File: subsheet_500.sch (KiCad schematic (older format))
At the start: 48 parts, among them J500 DM-15S — JOY0, J501 DM-15S — JOY1, U513 LM556_DUAL_TIMER_PHY, U514 LM556_DUAL_TIMER_PHY

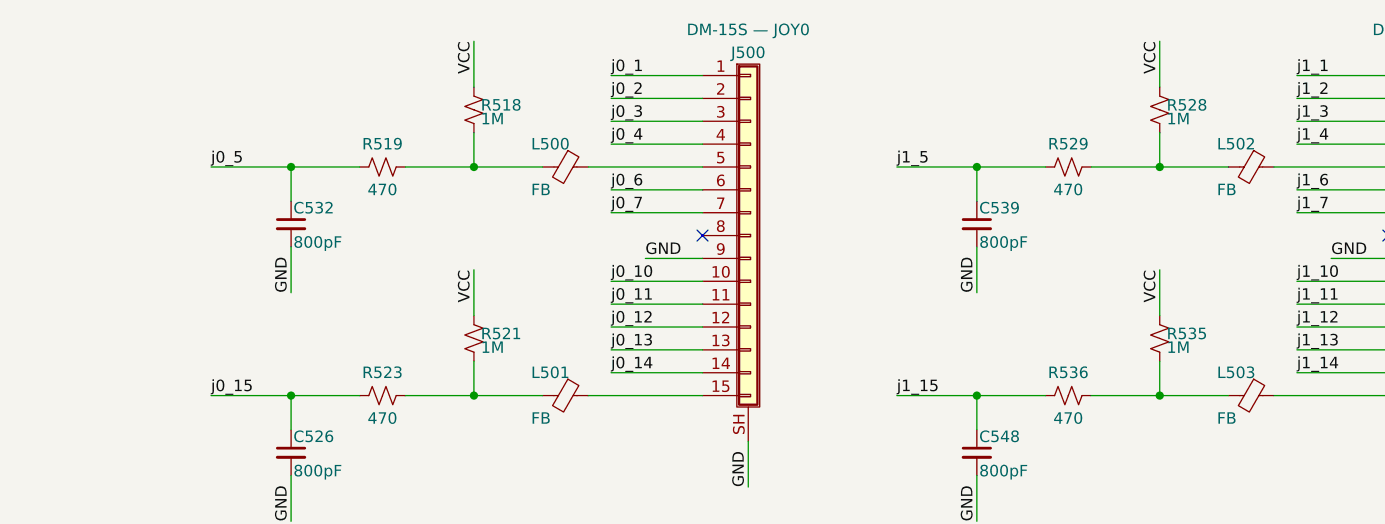
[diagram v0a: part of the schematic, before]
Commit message: [Schematics] added comment about the swap of the resistors between R518 and R521, and between R519 and R523
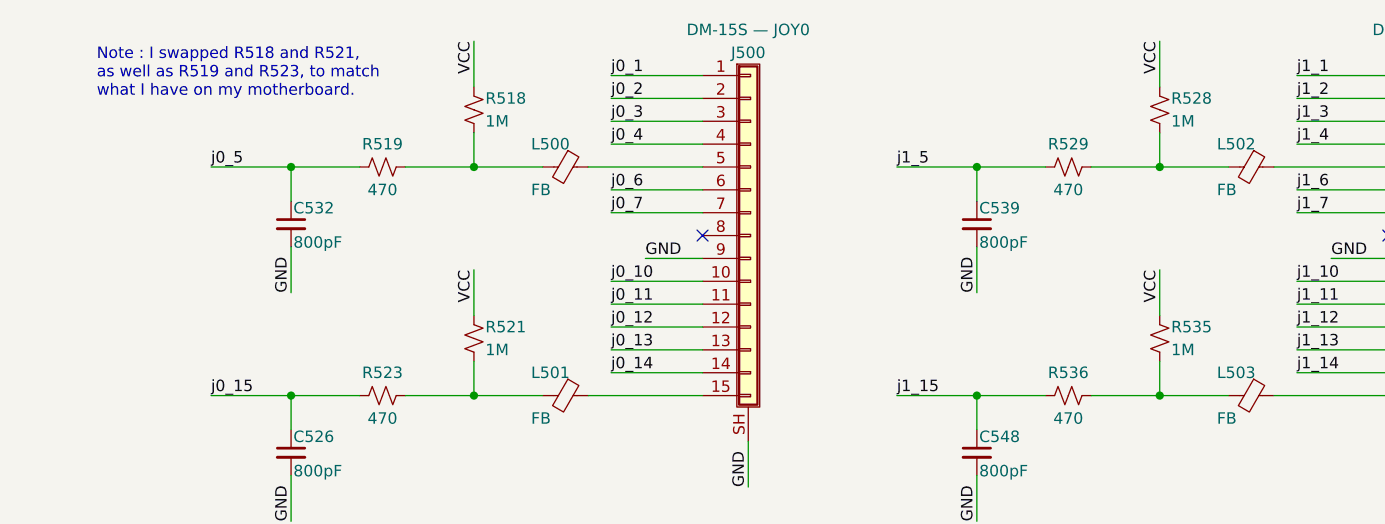
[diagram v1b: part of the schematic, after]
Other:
- note added: "Note : I swapped R518 and R521, \nas well as R519 and R523, to match \nwhat I have on my motherboard."
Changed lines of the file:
@@
 AR Path="/60B8B7AD/60CAB629" Ref="R?"  Part="1"
 AR Path="/60C451BA/60CAB629" Ref="R521"  Part="1"
-F 0 "R521" H 2680 2270 50  0000 L CNN
-F 1 "1M" H 2680 2210 50  0000 L CNN
+F 0 "R521" H 2700 2300 50  0000 L CNN
+F 1 "1M" H 2700 2200 50  0000 L CNN
 F 2 "commons_passives_THT:Passive_THT_resistor_W2.54mm_L12.70mm" H 2650 2250 50  0001 C CNN
 F 3 "~" H 2650 2250 50  0001 C CNN
@@
 AR Path="/60B8B7AD/60CB0FCA" Ref="R?"  Part="1"
 AR Path="/60C451BA/60CB0FCA" Ref="R518"  Part="1"
-F 0 "R518" H 2680 1270 50  0000 L CNN
-F 1 "1M" H 2680 1210 50  0000 L CNN
+F 0 "R518" H 2700 1300 50  0000 L CNN
+F 1 "1M" H 2700 1200 50  0000 L CNN
 F 2 "commons_passives_THT:Passive_THT_resistor_W2.54mm_L12.70mm" H 2650 1250 50  0001 C CNN
 F 3 "~" H 2650 1250 50  0001 C CNN
@@
 AR Path="/60B8B7AD/60CB29A8" Ref="R?"  Part="1"
 AR Path="/60C451BA/60CB29A8" Ref="R528"  Part="1"
-F 0 "R528" H 5680 1270 50  0000 L CNN
-F 1 "1M" H 5680 1210 50  0000 L CNN
+F 0 "R528" H 5700 1300 50  0000 L CNN
+F 1 "1M" H 5700 1200 50  0000 L CNN
 F 2 "commons_passives_THT:Passive_THT_resistor_W2.54mm_L12.70mm" H 5650 1250 50  0001 C CNN
 F 3 "~" H 5650 1250 50  0001 C CNN
@@
 AR Path="/60B8B7AD/60CB47EE" Ref="R?"  Part="1"
 AR Path="/60C451BA/60CB47EE" Ref="R535"  Part="1"
-F 0 "R535" H 5680 2270 50  0000 L CNN
-F 1 "1M" H 5680 2210 50  0000 L CNN
+F 0 "R535" H 5700 2300 50  0000 L CNN
+F 1 "1M" H 5700 2200 50  0000 L CNN
 F 2 "commons_passives_THT:Passive_THT_resistor_W2.54mm_L12.70mm" H 5650 2250 50  0001 C CNN
 F 3 "~" H 5650 2250 50  0001 C CNN
@@
 Wire Wire Line
 	6850 2900 6850 2700
+Text Notes 1000 1200 0    50   ~ 0
+Note : I swapped R518 and R521, \nas well as R519 and R523, to match \nwhat I have on my motherboard.
 $EndSCHEMATC

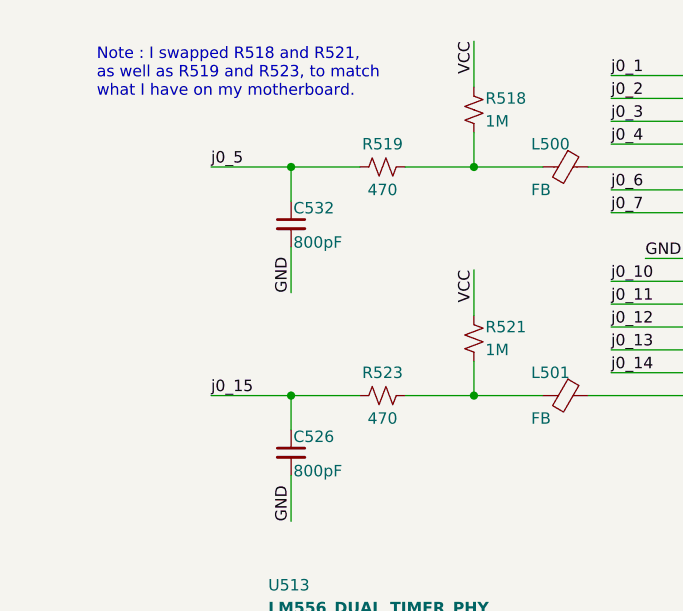
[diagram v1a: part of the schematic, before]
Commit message: [Schematic] Fixed again resistors connected to L500 and L501
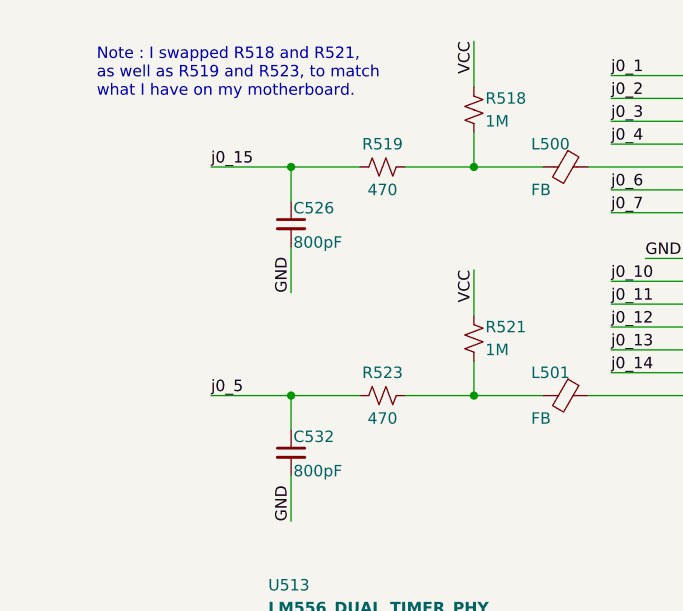
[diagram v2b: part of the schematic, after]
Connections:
- net j0_15: now also R519.2; no longer R523.2
- net j0_5: now also R523.2; no longer R519.2
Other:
- moved on the sheet: C526, C532
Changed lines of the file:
@@
 Text Label 3250 2400 0    50   ~ 0
 j0_14
-Text Label 1500 2500 0    50   ~ 0
+Text Label 1500 1500 0    50   ~ 0
 j0_15
 Text Label 3400 1900 0    50   ~ 0
@@
 L Device:C_Small C532
 U 1 1 60CCCD2F
+P 1850 2750
+F 0 "C532" H 1860 2820 50  0000 L CNN
+F 1 "800pF" H 1860 2670 50  0000 L CNN
+F 2 "commons_passives_THT:Passive_THT_capacitor_ceramic_radial_W5.08mm_L6.35mm_X11.43mm" H 1850 2750 50  0001 C CNN
+F 3 "~" H 1850 2750 50  0001 C CNN
+	1    1850 2750
+	1    0    0    -1
+$EndComp
+$Comp
+L Device:C_Small C526
+U 1 1 60CD0365
 P 1850 1750
-F 0 "C532" H 1860 1820 50  0000 L CNN
+F 0 "C526" H 1860 1820 50  0000 L CNN
 F 1 "800pF" H 1860 1670 50  0000 L CNN
 F 2 "commons_passives_THT:Passive_THT_capacitor_ceramic_radial_W5.08mm_L6.35mm_X11.43mm" H 1850 1750 50  0001 C CNN
 F 3 "~" H 1850 1750 50  0001 C CNN
 	1    1850 1750
-	1    0    0    -1
-$EndComp
-$Comp
-L Device:C_Small C526
-U 1 1 60CD0365
-P 1850 2750
-F 0 "C526" H 1860 2820 50  0000 L CNN
-F 1 "800pF" H 1860 2670 50  0000 L CNN
-F 2 "commons_passives_THT:Passive_THT_capacitor_ceramic_radial_W5.08mm_L6.35mm_X11.43mm" H 1850 2750 50  0001 C CNN
-F 3 "~" H 1850 2750 50  0001 C CNN
-	1    1850 2750
 	1    0    0    -1
 $EndComp
@@
 	1850 2650 1850 2500
 Wire Wire Line
-	1850 2500 2150 2500
-Wire Wire Line
 	1850 1650 1850 1500
 Wire Wire Line
 	1850 1500 2150 1500
-Text Label 1500 1500 0    50   ~ 0
+Text Label 1500 2500 0    50   ~ 0
 j0_5
 Wire Wire Line
@@
 Wire Wire Line
 	3350 3800 3250 3800
-Text Label 3700 3700 2    50   ~ 0
-j0_5
-Text Label 1000 3600 0    50   ~ 0
-j0_15
 Text Label 4500 3600 0    50   ~ 0
 j1_5
@@
 Text Notes 1000 1200 0    50   ~ 0
 Note : I swapped R518 and R521, \nas well as R519 and R523, to match \nwhat I have on my motherboard.
+Text Label 3700 3700 2    50   ~ 0
+j0_5
+Text Label 1000 3600 0    50   ~ 0
+j0_15
+Wire Wire Line
+	1850 2500 2150 2500
 $EndSCHEMATC
